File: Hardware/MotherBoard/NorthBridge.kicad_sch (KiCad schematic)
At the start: 4 parts, among them U6 74HC148, U7 74HC574, U8 ATF16V8B

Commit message: Fix
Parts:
- removed U8: ATF16V8B, Package_DIP:DIP-20_W7.62mm, symbol Logic_Programmable:GAL16V8
- added U8: ATF22V10B, Package_DIP:DIP-24_W7.62mm, symbol Logic_Programmable:PAL20RS10
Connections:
- net +5V: now also U6.10 (IO), U6.11 (I1), U8.24 (VCC); no longer U6.3 (I6), U6.4 (I7)
- net A10: now also U8.7 (I5)
- net A11: now also U8.6 (I4)
- net A12: now also U8.5 (I3)
- net A13: now also U8.4 (I2)
- net A14: now also U8.3 (I1)
- net A15: now also U8.2 (I0)
- net A8: now also U8.9 (I7)
- net A9: now also U8.8 (I6)
- net CLOCK: now also U8.1 (CLK)
- net DMAB: now also U8.11 (I9)
- net GND: now also U8.12 (GND), U8.13 (~OE~)
- net IOCSB: now also U8.23 (O0)
- net IRQ0B: now also U6.4 (I7); no longer U6.10 (IO)
- net IRQ1B: now also U6.3 (I6); no longer U6.11 (I1)
- net PORT1B: now also U8.22 (O1)
- net PORT2B: now also U8.21 (O2)
- net RAMCSB: now also U8.19 (O4)
- net ROMCSB: now also U8.18 (O5)
- net at U7.1 (OE): now also U8.20 (O3)
- new net DMARW: U8.17 (O6)
- new net RW: U8.10 (I8)
- no-connect marks 3 -> 4
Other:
- title: Retro 6502 Mother Board -> Miniish
- moved on the sheet: C9

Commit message: New motherboard version
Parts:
- removed C9: 220nF, Capacitor_THT:C_Disc_D5.0mm_W2.5mm_P5.00mm, symbol Device:C_Small
- removed U6: 74HC148, Package_DIP:DIP-16_W7.62mm, symbol 74xx:74LS148
- removed U7: 74HC574, Package_DIP:DIP-20_W7.62mm, symbol 74xx:74HCT574
- removed U8: ATF22V10B, Package_DIP:DIP-24_W7.62mm, symbol Logic_Programmable:PAL20RS10
- added C5: 10uF, Capacitor_THT:C_Radial_D5.0mm_H11.0mm_P2.00mm, symbol Device:C_Small
- added C6, C7: 100nF, Capacitor_THT:C_Disc_D5.0mm_W2.5mm_P2.50mm, symbol Device:C_Small
- added C8: 470nF, Capacitor_THT:C_Disc_D5.0mm_W2.5mm_P5.00mm, symbol Device:C_Small
- added D2: 1N4001, Diode_THT:D_DO-41_SOD81_P10.16mm_Horizontal, symbol Diode:1N4001
- added J12: NMI_PULLUP, Connector_PinHeader_2.54mm:PinHeader_1x02_P2.54mm_Vertical, symbol Connector:Conn_01x02_Pin
- added J6: DMA_PULLUP, Connector_PinHeader_2.54mm:PinHeader_1x02_P2.54mm_Vertical, symbol Connector:Conn_01x02_Pin
- added R1 (x2), R5: 3K3, Resistor_THT:R_Axial_DIN0207_L6.3mm_D2.5mm_P10.16mm_Horizontal, symbol Device:R
- added R3: 10K, Resistor_THT:R_Axial_DIN0207_L6.3mm_D2.5mm_P10.16mm_Horizontal, symbol Device:R_Small
- added SW1: RESET_SW, Button_Switch_THT:SW_Tactile_SPST_Angled_PTS645Vx83-2LFS, symbol Switch:SW_Push
- added U3: AS6C62256, Package_DIP:DIP-28_W15.24mm, symbol Memory_RAM:HM62256BLP
- added U4: WD65C02, Package_DIP:DIP-40_W15.24mm, symbol 65xx:WD65C02
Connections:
- net +5V: now also C5.1, C6.1, C7.1, R1.2, R1.2, R3.1, R5.1, U3.28 (VCC), U4.8 (VCC)
- net A10: now also U3.21 (A10), U4.19 (A10)
- net A11: now also U3.23 (A11), U4.20 (A11)
- net A12: now also U3.2 (A12), U4.22 (A12)
- net A13: now also U3.26 (A13), U4.23 (A13)
- net A14: now also U3.1 (A14), U4.24 (A14)
- net A15: now also U4.25 (A15)
- net A8: now also U3.25 (A8), U4.17 (A8)
- net A9: now also U3.24 (A9), U4.18 (A9)
- net CLOCK: now also U4.37 (PHI2)
- net D0: now also U3.11 (Q0), U4.33 (D0)
- net D1: now also U3.12 (Q1), U4.32 (D1)
- net D2: now also U3.13 (Q2), U4.31 (D2)
- net D3: now also U3.15 (Q3), U4.30 (D3)
- net D4: now also U3.16 (Q4), U4.29 (D4)
- net D5: now also U3.17 (Q5), U4.28 (D5)
- net D6: now also U3.18 (Q6), U4.27 (D6)
- net D7: now also U3.19 (Q7), U4.26 (D7)
- net DMAB: now also D2.1 (K), J6.1 (Pin_1), U4.36 (BE)
- net GND: now also C5.2, C6.2, C7.2, C8.2, SW1.2, U3.14 (GND), U3.22 (~{OE}), U4.21 (GND)
- net IRQB: now also U4.4 (~{IRQ})
- net RAMCSB: now also U3.20 (~{CS})
- net RW: now also U3.27 (~{WE}), U4.34 (R/~{W})
- new net: J12.2 (Pin_2), R1.1
- new net A0: U3.10 (A0), U4.9 (A0)
- new net A1: U3.9 (A1), U4.10 (A1)
- new net A2: U3.8 (A2), U4.11 (A2)
- new net A3: U3.7 (A3), U4.12 (A3)
- new net A4: U3.6 (A4), U4.13 (A4)
- new net A5: U3.5 (A5), U4.14 (A5)
- new net A6: U3.4 (A6), U4.15 (A6)
- new net A7: U3.3 (A7), U4.16 (A7)
- new net NMIB: J12.1 (Pin_1), U4.6 (~{NMI})
- new net RDY: D2.2 (A), J6.2 (Pin_2), R1.1, U4.2 (RDY)
- new net RESET: C8.1, R3.2, SW1.1, U4.40 (~{RESET})
- new net SOB: R5.2, U4.38 (~{SO})
- no-connect marks 4 -> 5
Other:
- note added: "CPU"
- note added: "Decouplings and Pullups"
- note added: "RAM"
- note added: "Reset"
- note removed: "Controller Hub"
- note removed: "Decoder IRQ"

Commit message: Finalize 1.3
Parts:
- removed R5: 3K3, Resistor_THT:R_Axial_DIN0207_L6.3mm_D2.5mm_P10.16mm_Horizontal, symbol Device:R
- added R1 (x2): 3K3, Resistor_THT:R_Axial_DIN0207_L6.3mm_D2.5mm_P10.16mm_Horizontal, symbol Device:R
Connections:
- net +5V: now also R1.2, R1.2
- net RDY: now also R1.1; no longer J6.2 (Pin_2), R1.1
- net SOB: now also R1.1
- new net: J6.2 (Pin_2), R1.1
- no-connect marks 5 -> 6

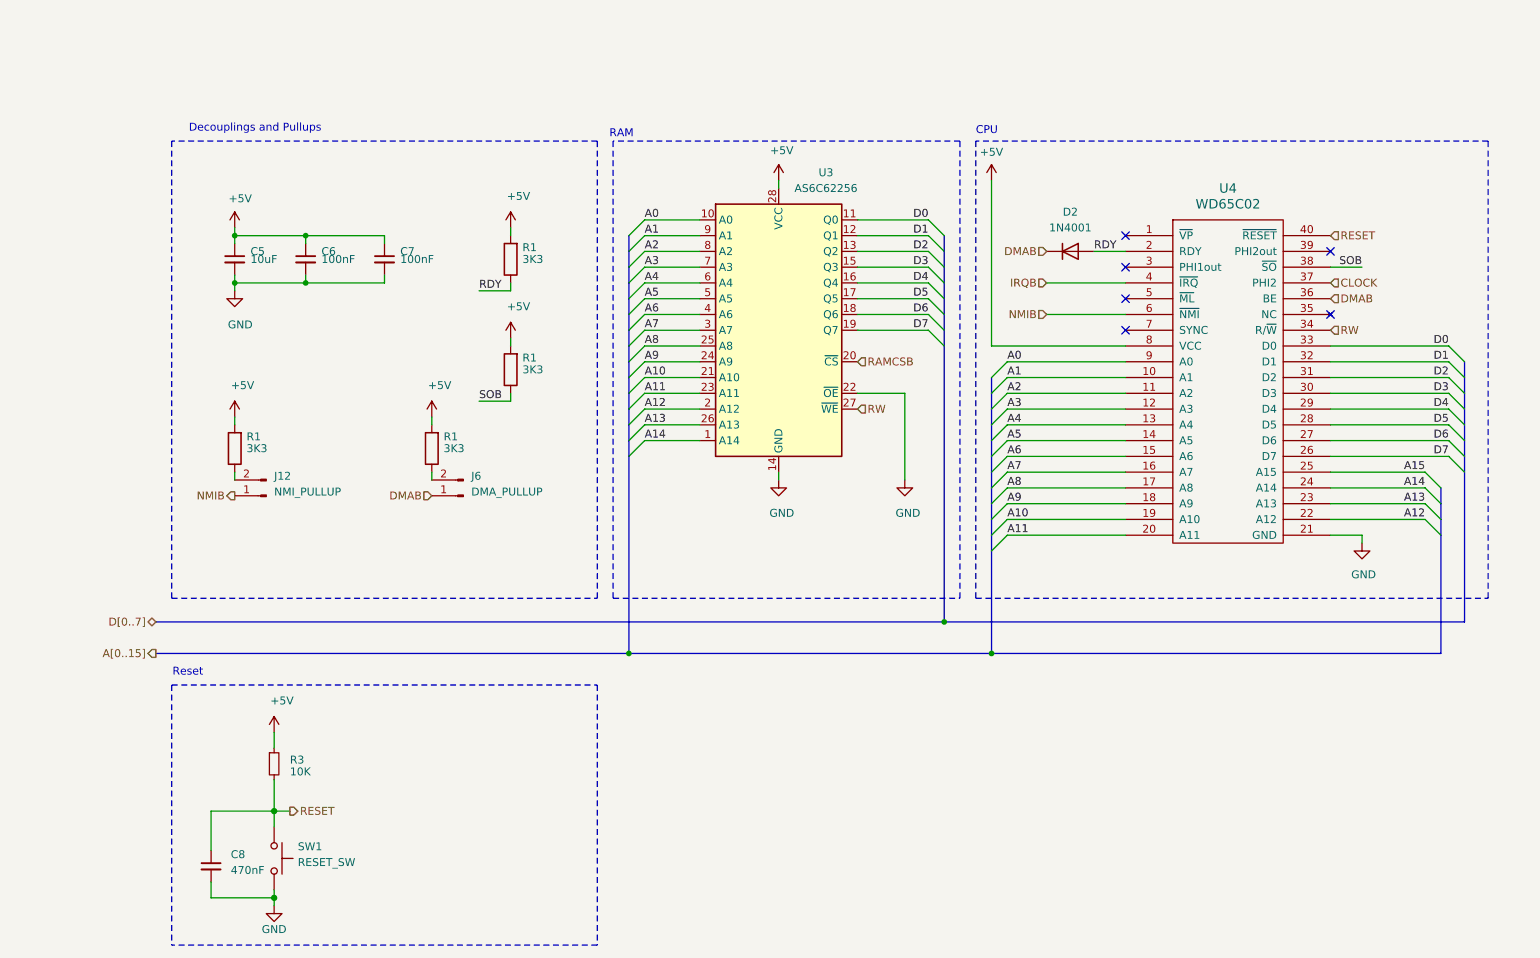
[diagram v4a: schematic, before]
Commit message: Add SPI Board
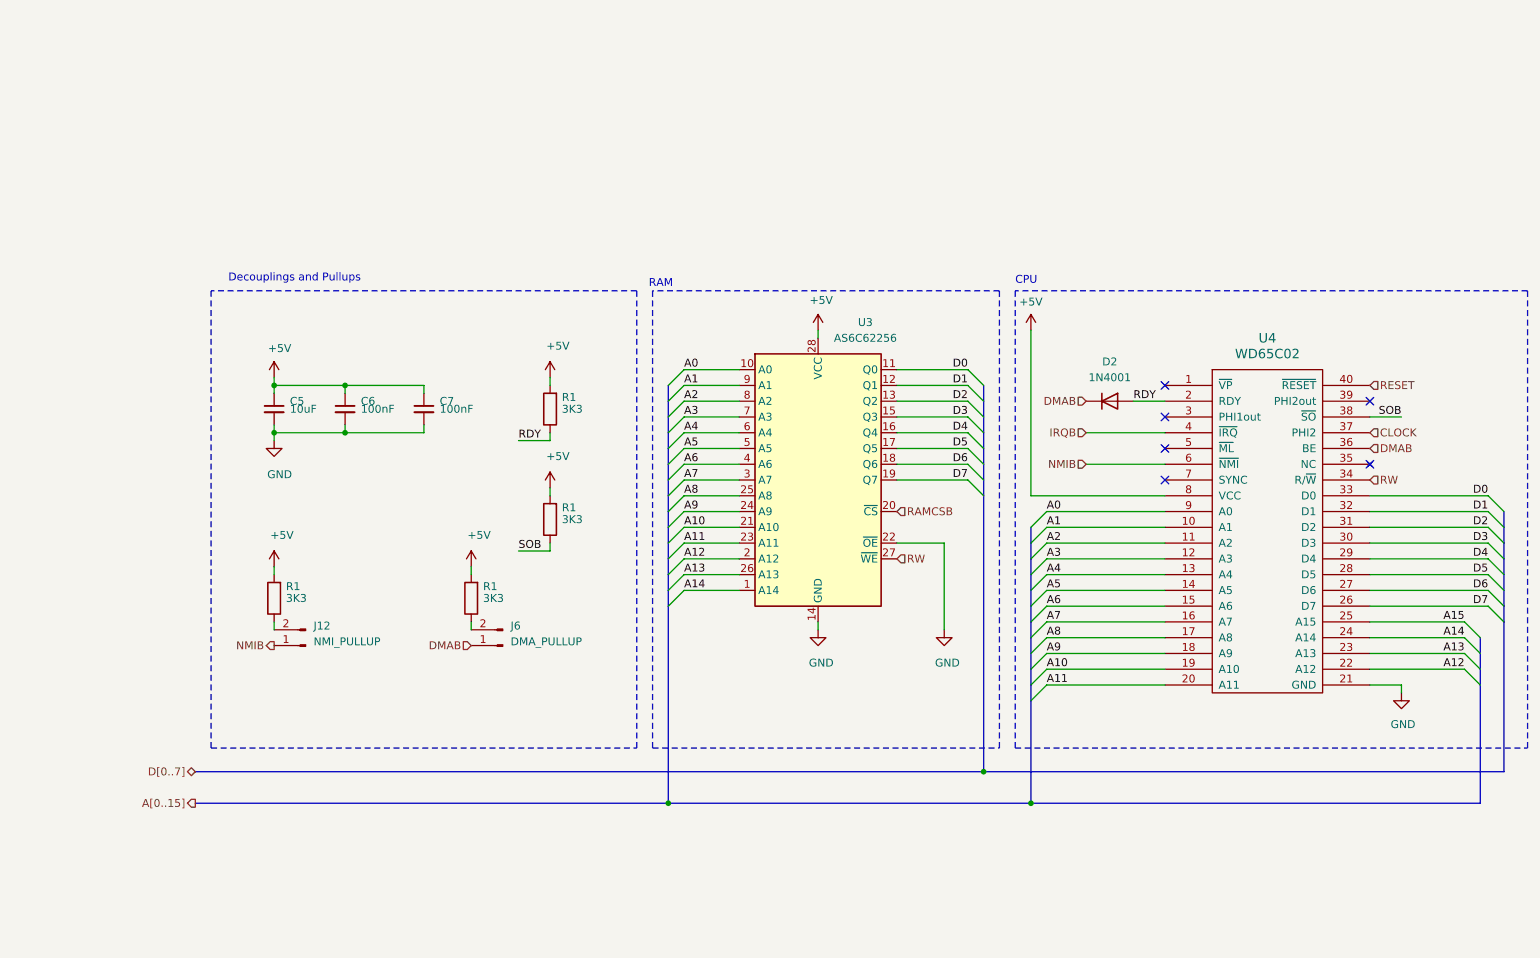
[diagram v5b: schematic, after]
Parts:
- removed C8: 470nF, Capacitor_THT:C_Disc_D5.0mm_W2.5mm_P5.00mm, symbol Device:C_Small
- removed R3: 10K, Resistor_THT:R_Axial_DIN0207_L6.3mm_D2.5mm_P10.16mm_Horizontal, symbol Device:R_Small
- removed SW1: RESET_SW, Button_Switch_THT:SW_Tactile_SPST_Angled_PTS645Vx83-2LFS, symbol Switch:SW_Push
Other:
- note removed: "Reset"
- moved on the sheet: C5, C6, C7, D2, J12, J6, R1, U3, U4

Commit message: A lot of new hardware
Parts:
- J12: value NMI_PULLUP -> NMI
- J6: value DMA_PULLUP -> DMA
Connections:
- no-connect marks 6 -> 5
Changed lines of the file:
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@@
   (junction (at 67.31 82.55) (diameter 0) (color 0 0 0 0)
   )
-  (no_connect (at 232.41 87.63))
   (no_connect (at 199.39 80.01))
   (no_connect (at 232.41 77.47))
@@
       (effects (font (size 1.27 1.27)) (justify right))
     )
-    (property "Value" "NMI_PULLUP" (at 62.23 116.205 0)
+    (property "Value" "NMI" (at 62.23 116.205 0)
       (effects (font (size 1.27 1.27)) (justify right))
     )
@@
       (effects (font (size 1.27 1.27)) (justify right))
     )
-    (property "Value" "DMA_PULLUP" (at 93.98 116.205 0)
+    (property "Value" "DMA" (at 93.98 116.205 0)
       (effects (font (size 1.27 1.27)) (justify right))
     )

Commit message: Add ArduinoMultiInterface
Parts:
- renumbered J12 to J5, R1 to R11, R1 to R12, R1 to R2, R1 to R4
